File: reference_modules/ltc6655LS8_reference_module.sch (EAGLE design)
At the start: 8 parts

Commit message: * finished ltc6655 reference board
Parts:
- removed C2: 10u, SquantorRCL:C-EUC0805
- added R1: (no value), SquantorRCL:R-EU_R1206
- added R2: ferrite, SquantorRCL:R-EU_R0805
- C3: value 2.2u -> 10u; device SquantorRCL:C-EUC2824W -> SquantorRCL:C-EUC0805
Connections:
- new net N$1: JP1.1, R2.1
- net GND: now also C3.1; no longer C2.2, C3.2
- net VCC_VREF: now also C3.2, R2.2; no longer C2.1, JP1.1
- net VREF_IN: now also R1.2
- net VREF_OUT: now also R1.1; no longer C3.1
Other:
- moved on the sheet: C3
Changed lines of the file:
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@@
 <layer number="115" name="ReferenceISLANDS" color="7" fill="1" visible="yes" active="yes"/>
 <layer number="116" name="Patch_BOT" color="9" fill="4" visible="yes" active="yes"/>
+<layer number="117" name="BACKMAAT1" color="7" fill="1" visible="yes" active="yes"/>
 <layer number="118" name="Rect_Pads" color="7" fill="1" visible="yes" active="yes"/>
+<layer number="119" name="KAP_TEKEN" color="7" fill="1" visible="yes" active="yes"/>
+<layer number="120" name="KAP_MAAT1" color="7" fill="1" visible="yes" active="yes"/>
 <layer number="121" name="_tsilk" color="7" fill="1" visible="yes" active="yes"/>
 <layer number="122" name="_bsilk" color="7" fill="1" visible="yes" active="yes"/>
@@
 <layer number="128" name="_bValues" color="7" fill="1" visible="yes" active="yes"/>
 <layer number="129" name="Mask" color="7" fill="1" visible="yes" active="yes"/>
+<layer number="130" name="SMDSTROOK" color="7" fill="1" visible="yes" active="yes"/>
 <layer number="131" name="tAdjust" color="7" fill="1" visible="yes" active="yes"/>
 <layer number="132" name="bAdjust" color="7" fill="1" visible="yes" active="yes"/>
+<layer number="133" name="BGA_CORE_SUP" color="12" fill="1" visible="yes" active="yes"/>
+<layer number="134" name="BGA_GND" color="1" fill="1" visible="yes" active="yes"/>
+<layer number="135" name="BGA_NC" color="8" fill="1" visible="yes" active="yes"/>
+<layer number="136" name="BGA_DED" color="14" fill="1" visible="yes" active="yes"/>
 <layer number="144" name="Drill_legend" color="7" fill="1" visible="yes" active="yes"/>
 <layer number="150" name="Notes" color="7" fill="1" visible="yes" active="yes"/>
@@
 <part name="JP2" library="SquantorConnectors" deviceset="PINHD-1X10" device="NORM_OCT"/>
 <part name="U$1" library="SquantorLinearTechnology" deviceset="LTC6655" device="LS8_ELONG"/>
-<part name="C2" library="SquantorRCL" deviceset="C-EU" device="C0805" value="10u"/>
 <part name="C1" library="SquantorRCL" deviceset="C-EU" device="C0603" value="100n"/>
-<part name="C3" library="SquantorRCL" deviceset="C-EU" device="C2824W" value="2.2u"/>
 <part name="C4" library="SquantorRCL" deviceset="C-EU" device="C2824W" value="2.2u"/>
 <part name="C5" library="SquantorRCL" deviceset="C-EU" device="C2824W" value="2.2u"/>
@@
 <part name="GND3" library="supply1" deviceset="GND" device=""/>
 <part name="GND4" library="supply1" deviceset="GND" device=""/>
+<part name="R1" library="SquantorRCL" deviceset="R-EU_" device="R1206"/>
+<part name="R2" library="SquantorRCL" deviceset="R-EU_" device="R0805" value="ferrite"/>
+<part name="C3" library="SquantorRCL" deviceset="C-EU" device="C0805" value="10u"/>
+<part name="GND5" library="supply1" deviceset="GND" device=""/>
 </parts>
 <sheets>
@@
 <instance part="JP2" gate="A" x="134.62" y="30.48" rot="MR180"/>
 <instance part="U$1" gate="G$1" x="71.12" y="27.94"/>
-<instance part="C2" gate="G$1" x="71.12" y="83.82" rot="R270"/>
 <instance part="C1" gate="G$1" x="71.12" y="76.2" rot="R270"/>
-<instance part="C3" gate="G$1" x="71.12" y="68.58" rot="R270"/>
 <instance part="C4" gate="G$1" x="71.12" y="60.96" rot="R270"/>
 <instance part="C5" gate="G$1" x="71.12" y="53.34" rot="R270"/>
@@
 <instance part="GND3" gate="1" x="48.26" y="22.86" rot="R270"/>
 <instance part="GND4" gate="1" x="71.12" y="48.26" rot="R180"/>
+<instance part="R1" gate="G$1" x="106.68" y="63.5" rot="R90"/>
+<instance part="R2" gate="G$1" x="25.4" y="50.8" rot="R90"/>
+<instance part="C3" gate="G$1" x="17.78" y="58.42" rot="R90"/>
+<instance part="GND5" gate="1" x="12.7" y="58.42" rot="R270"/>
 </instances>
 <busses>
@@
 <nets>
 <net name="VCC_VREF" class="0">
-<segment>
-<pinref part="JP1" gate="A" pin="1"/>
-<wire x1="17.78" y1="43.18" x2="22.86" y2="43.18" width="0.1524" layer="91"/>
-<label x="22.86" y="43.18" size="1.778" layer="95"/>
-</segment>
-<segment>
-<pinref part="C2" gate="G$1" pin="1"/>
-<wire x1="73.66" y1="83.82" x2="76.2" y2="83.82" width="0.1524" layer="91"/>
-<label x="76.2" y="83.82" size="1.778" layer="95"/>
-</segment>
 <segment>
 <pinref part="C1" gate="G$1" pin="1"/>
@@
 <label x="50.8" y="35.56" size="1.778" layer="95" rot="R180"/>
 </segment>
+<segment>
+<pinref part="R2" gate="G$1" pin="2"/>
+<wire x1="25.4" y1="55.88" x2="25.4" y2="58.42" width="0.1524" layer="91"/>
+<pinref part="C3" gate="G$1" pin="2"/>
+<wire x1="25.4" y1="58.42" x2="22.86" y2="58.42" width="0.1524" layer="91"/>
+<label x="25.4" y="58.42" size="1.778" layer="95"/>
+</segment>
 </net>
 <net name="VREF_IN" class="0">
@@
 <label x="93.98" y="30.48" size="1.778" layer="95"/>
 </segment>
+<segment>
+<pinref part="R1" gate="G$1" pin="2"/>
+<wire x1="106.68" y1="68.58" x2="106.68" y2="71.12" width="0.1524" layer="91"/>
+<label x="106.68" y="71.12" size="1.778" layer="95" rot="R90"/>
+</segment>
 </net>
 <net name="VREF_OUT" class="0">
@@
 </segment>
 <segment>
-<pinref part="C3" gate="G$1" pin="1"/>
-<wire x1="73.66" y1="68.58" x2="76.2" y2="68.58" width="0.1524" layer="91"/>
-<wire x1="76.2" y1="68.58" x2="76.2" y2="60.96" width="0.1524" layer="91"/>
 <pinref part="C5" gate="G$1" pin="1"/>
 <wire x1="76.2" y1="60.96" x2="76.2" y2="53.34" width="0.1524" layer="91"/>
@@
 <pinref part="C4" gate="G$1" pin="1"/>
 <wire x1="73.66" y1="60.96" x2="76.2" y2="60.96" width="0.1524" layer="91"/>
-<junction x="76.2" y="60.96"/>
 <label x="76.2" y="60.96" size="1.778" layer="95"/>
+</segment>
+<segment>
+<pinref part="R1" gate="G$1" pin="1"/>
+<wire x1="106.68" y1="58.42" x2="106.68" y2="55.88" width="0.1524" layer="91"/>
+<label x="106.68" y="55.88" size="1.778" layer="95" rot="R270"/>
 </segment>
 </net>
@@
 </segment>
 <segment>
-<pinref part="C3" gate="G$1" pin="2"/>
-<wire x1="66.04" y1="68.58" x2="63.5" y2="68.58" width="0.1524" layer="91"/>
-<wire x1="63.5" y1="68.58" x2="63.5" y2="60.96" width="0.1524" layer="91"/>
 <pinref part="C5" gate="G$1" pin="2"/>
 <wire x1="63.5" y1="60.96" x2="63.5" y2="53.34" width="0.1524" layer="91"/>
@@
 <pinref part="C4" gate="G$1" pin="2"/>
 <wire x1="63.5" y1="60.96" x2="66.04" y2="60.96" width="0.1524" layer="91"/>
-<junction x="63.5" y="60.96"/>
 <label x="63.5" y="60.96" size="1.778" layer="95" rot="R180"/>
 </segment>
@@
 </segment>
 <segment>
-<pinref part="C2" gate="G$1" pin="2"/>
-<wire x1="66.04" y1="83.82" x2="63.5" y2="83.82" width="0.1524" layer="91"/>
-<label x="63.5" y="83.82" size="1.778" layer="95" rot="R180"/>
+<pinref part="C3" gate="G$1" pin="1"/>
+<pinref part="GND5" gate="1" pin="GND"/>
 </segment>
 </net>
@@
 </segment>
 </net>
+<net name="N$1" class="0">
+<segment>
+<pinref part="JP1" gate="A" pin="1"/>
+<wire x1="17.78" y1="43.18" x2="25.4" y2="43.18" width="0.1524" layer="91"/>
+<pinref part="R2" gate="G$1" pin="1"/>
+<wire x1="25.4" y1="43.18" x2="25.4" y2="45.72" width="0.1524" layer="91"/>
+</segment>
+</net>

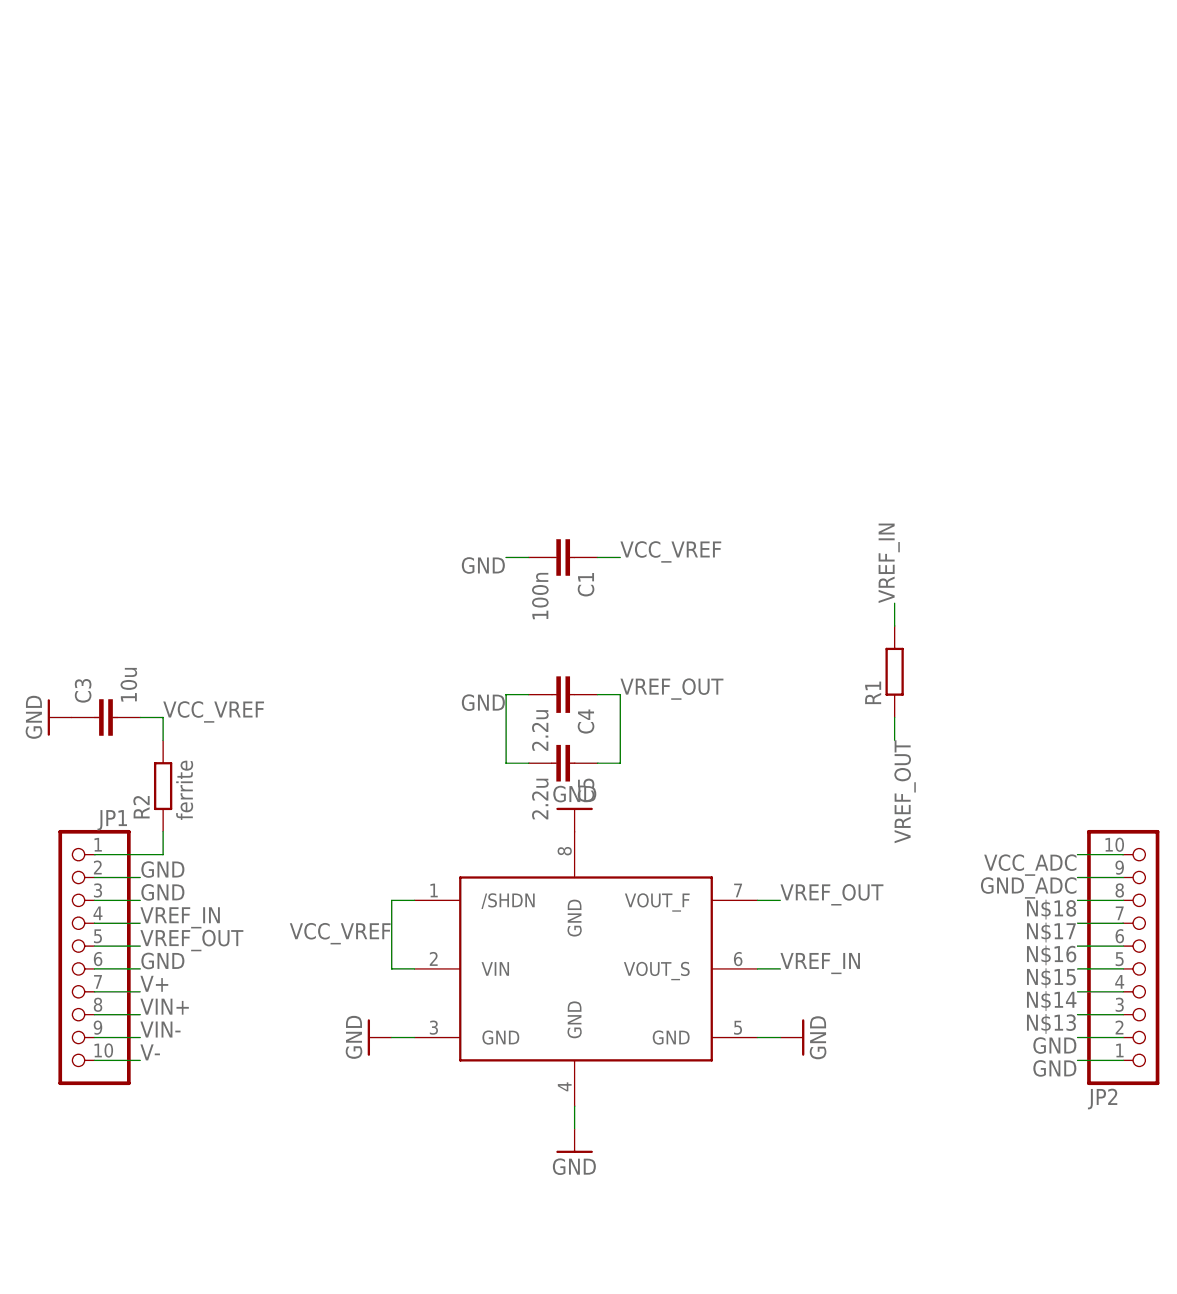
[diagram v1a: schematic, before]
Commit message: * removed old unused project * switched to module outline layout, this way i am sure the boards will remain the same
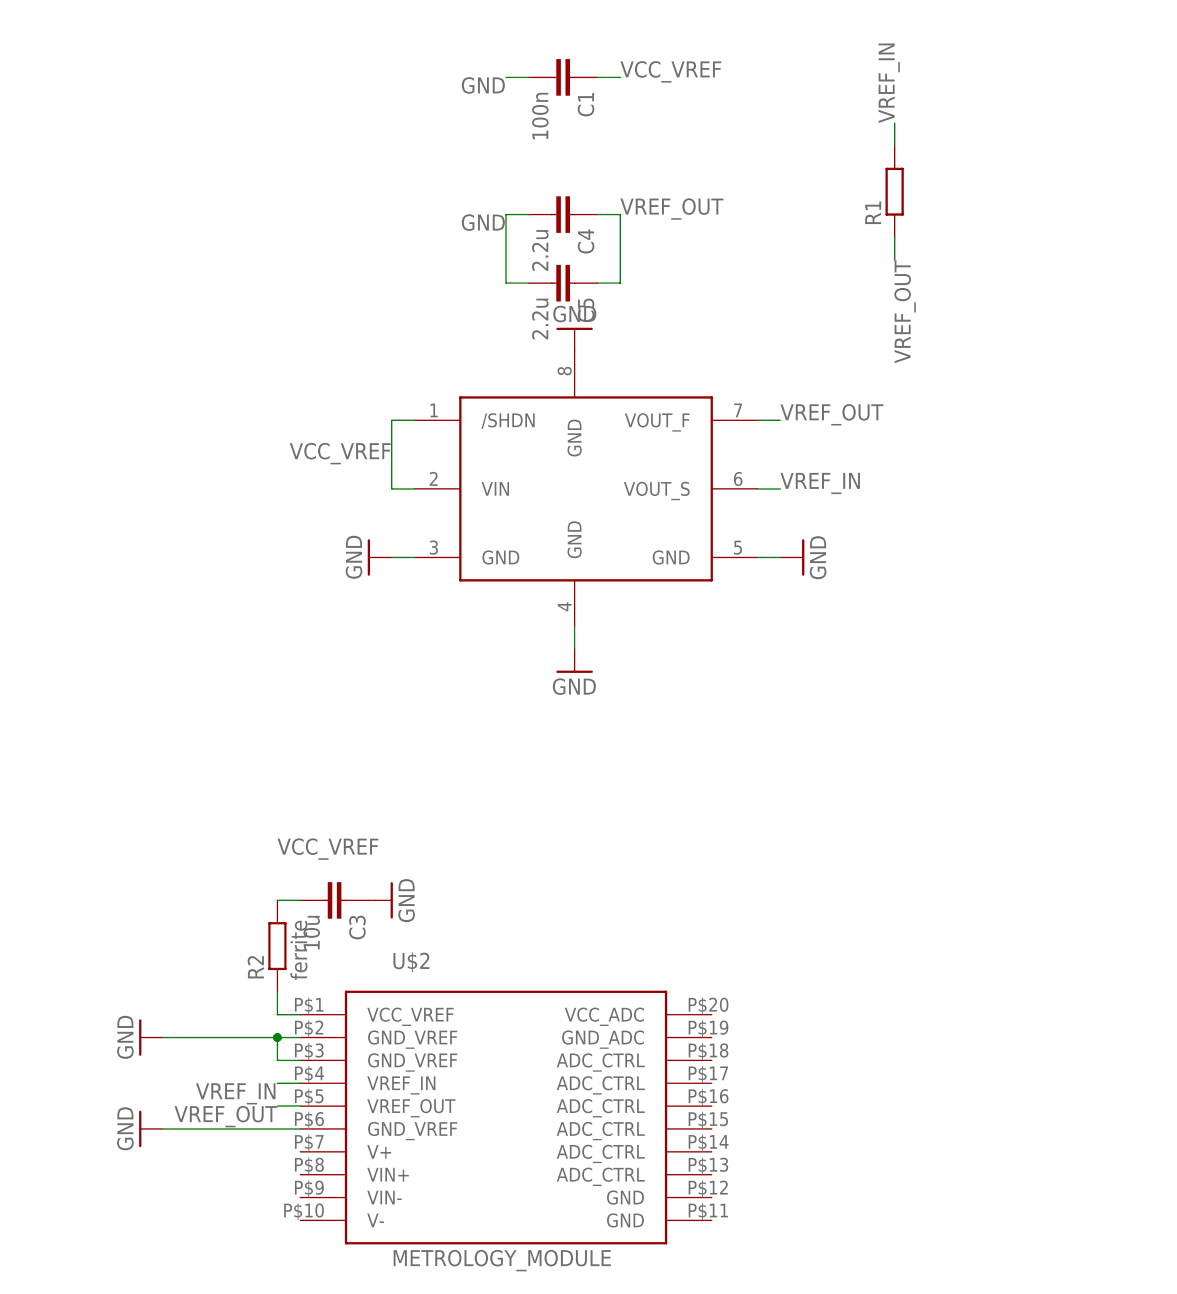
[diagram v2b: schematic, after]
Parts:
- removed JP1, JP2: (no value), SquantorConnectors:PINHD-1X10NORM_OCT
- added U$2: METROLOGY_MODULE, SquantorPCBOutline:METROLOGY_MODULE
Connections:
- removed net GND_ADC: JP2.9
- removed net N$13: JP2.3
- removed net N$14: JP2.4
- removed net N$15: JP2.5
- removed net N$16: JP2.6
- removed net N$17: JP2.7
- removed net N$18: JP2.8
- removed net V+: JP1.7
- removed net V-: JP1.10
- removed net VCC_ADC: JP2.10
- removed net VIN+: JP1.8
- removed net VIN-: JP1.9
- net GND: now also U$2.GND_VREF@2, U$2.GND_VREF@3, U$2.GND_VREF@6; no longer JP1.2, JP1.3, JP1.6, JP2.1, JP2.2
- net N$1: now also U$2.VCC_VREF@1; no longer JP1.1
- net VREF_IN: now also U$2.VREF_IN@4; no longer JP1.4
- net VREF_OUT: now also U$2.VREF_OUT@5; no longer JP1.5
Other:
- moved on the sheet: C1, C3, C4, C5, R1, R2

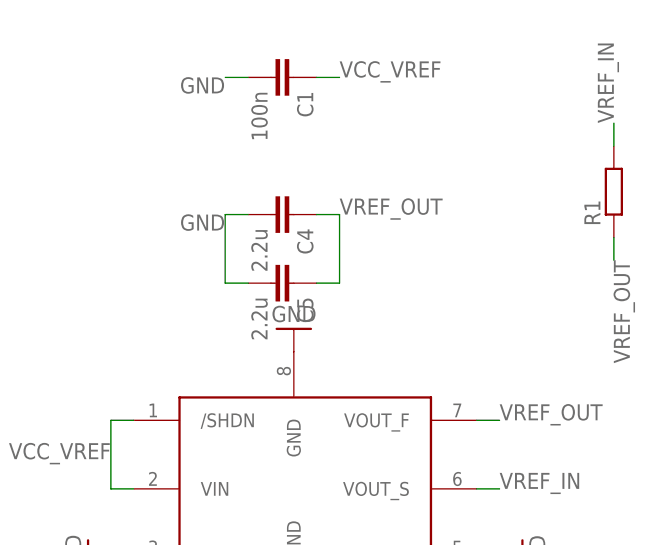
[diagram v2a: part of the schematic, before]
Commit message: * updated board format * made the LTC6655 reference module more compact, hopefully better * small modifications to the MCP355X ADC module
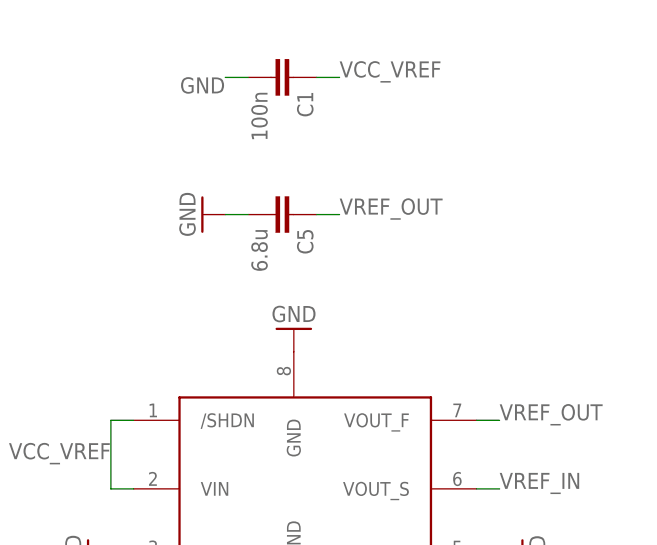
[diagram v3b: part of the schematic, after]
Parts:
- removed C4: 2.2u, SquantorRCL:C-EUC2824W
- removed R1: (no value), SquantorRCL:R-EU_R1206
- C5: value 2.2u -> 6.8u; device SquantorRCL:C-EUC2824W -> SquantorRCL:C-EU050-075X075
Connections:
- net GND: no longer C4.2
- net VREF_IN: no longer R1.2
- net VREF_OUT: no longer C4.1, R1.1
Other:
- moved on the sheet: C5
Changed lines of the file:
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@@
 <part name="U$1" library="SquantorLinearTechnology" deviceset="LTC6655" device="LS8_ELONG"/>
 <part name="C1" library="SquantorRCL" deviceset="C-EU" device="C0603" value="100n"/>
-<part name="C4" library="SquantorRCL" deviceset="C-EU" device="C2824W" value="2.2u"/>
-<part name="C5" library="SquantorRCL" deviceset="C-EU" device="C2824W" value="2.2u"/>
+<part name="C5" library="SquantorRCL" deviceset="C-EU" device="050-075X075" value="6.8u"/>
 <part name="GND1" library="supply1" deviceset="GND" device=""/>
 <part name="GND2" library="supply1" deviceset="GND" device=""/>
 <part name="GND3" library="supply1" deviceset="GND" device=""/>
 <part name="GND4" library="supply1" deviceset="GND" device=""/>
-<part name="R1" library="SquantorRCL" deviceset="R-EU_" device="R1206"/>
 <part name="R2" library="SquantorRCL" deviceset="R-EU_" device="R0805" value="ferrite"/>
 <part name="C3" library="SquantorRCL" deviceset="C-EU" device="C0805" value="10u"/>
@@
 <part name="GND6" library="supply1" deviceset="GND" device=""/>
 <part name="GND7" library="supply1" deviceset="GND" device=""/>
+<part name="GND8" library="supply1" deviceset="GND" device=""/>
 </parts>
 <sheets>
@@
 <instance part="U$1" gate="G$1" x="71.12" y="81.28"/>
 <instance part="C1" gate="G$1" x="71.12" y="129.54" rot="R270"/>
-<instance part="C4" gate="G$1" x="71.12" y="114.3" rot="R270"/>
-<instance part="C5" gate="G$1" x="71.12" y="106.68" rot="R270"/>
+<instance part="C5" gate="G$1" x="71.12" y="114.3" rot="R270"/>
 <instance part="GND1" gate="1" x="71.12" y="63.5"/>
 <instance part="GND2" gate="1" x="96.52" y="76.2" rot="R90"/>
 <instance part="GND3" gate="1" x="48.26" y="76.2" rot="R270"/>
 <instance part="GND4" gate="1" x="71.12" y="101.6" rot="R180"/>
-<instance part="R1" gate="G$1" x="106.68" y="116.84" rot="R90"/>
 <instance part="R2" gate="G$1" x="38.1" y="33.02" rot="R90"/>
 <instance part="C3" gate="G$1" x="45.72" y="38.1" rot="R270"/>
@@
 <instance part="GND6" gate="1" x="22.86" y="22.86" rot="R270"/>
 <instance part="GND7" gate="1" x="22.86" y="12.7" rot="R270"/>
+<instance part="GND8" gate="1" x="60.96" y="114.3" rot="R270"/>
 </instances>
 <busses>
@@
 <label x="93.98" y="83.82" size="1.778" layer="95"/>
 </segment>
-<segment>
-<pinref part="R1" gate="G$1" pin="2"/>
-<wire x1="106.68" y1="121.92" x2="106.68" y2="124.46" width="0.1524" layer="91"/>
-<label x="106.68" y="124.46" size="1.778" layer="95" rot="R90"/>
-</segment>
 </net>
 <net name="VREF_OUT" class="0">
@@
 <segment>
 <pinref part="C5" gate="G$1" pin="1"/>
-<wire x1="76.2" y1="114.3" x2="76.2" y2="106.68" width="0.1524" layer="91"/>
-<wire x1="76.2" y1="106.68" x2="73.66" y2="106.68" width="0.1524" layer="91"/>
-<pinref part="C4" gate="G$1" pin="1"/>
-<wire x1="73.66" y1="114.3" x2="76.2" y2="114.3" width="0.1524" layer="91"/>
+<wire x1="76.2" y1="114.3" x2="73.66" y2="114.3" width="0.1524" layer="91"/>
 <label x="76.2" y="114.3" size="1.778" layer="95"/>
-</segment>
-<segment>
-<pinref part="R1" gate="G$1" pin="1"/>
-<wire x1="106.68" y1="111.76" x2="106.68" y2="109.22" width="0.1524" layer="91"/>
-<label x="106.68" y="109.22" size="1.778" layer="95" rot="R270"/>
 </segment>
 </net>
@@
 <segment>
 <pinref part="C5" gate="G$1" pin="2"/>
-<wire x1="63.5" y1="114.3" x2="63.5" y2="106.68" width="0.1524" layer="91"/>
-<wire x1="63.5" y1="106.68" x2="66.04" y2="106.68" width="0.1524" layer="91"/>
-<pinref part="C4" gate="G$1" pin="2"/>
 <wire x1="63.5" y1="114.3" x2="66.04" y2="114.3" width="0.1524" layer="91"/>
-<label x="63.5" y="114.3" size="1.778" layer="95" rot="R180"/>
+<pinref part="GND8" gate="1" pin="GND"/>
 </segment>
 <segment>

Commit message: * modified boards and processed for production
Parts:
- C5: device SquantorRCL:C-EU050-075X075 -> SquantorRCL:C-EU050-085X075W
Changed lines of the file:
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@@
 <part name="U$1" library="SquantorLinearTechnology" deviceset="LTC6655" device="LS8_ELONG"/>
 <part name="C1" library="SquantorRCL" deviceset="C-EU" device="C0603" value="100n"/>
-<part name="C5" library="SquantorRCL" deviceset="C-EU" device="050-075X075" value="6.8u"/>
+<part name="C5" library="SquantorRCL" deviceset="C-EU" device="050-085X075W" value="6.8u"/>
 <part name="GND1" library="supply1" deviceset="GND" device=""/>
 <part name="GND2" library="supply1" deviceset="GND" device=""/>
